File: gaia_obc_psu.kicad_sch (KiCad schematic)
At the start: 74 parts, among them IC1 MAX17048G+T10, Q2 FS8205A, SW8 SW_Slide_DPDT, U10 TPS22917DBV, U11 AP2112K-3.3, U12 DW01A, U13 AP2112K-3.0, U14 LGS4056HDB, U4 INA3221, U5 INA3221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

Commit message: obc v1.2-pre1
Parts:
- removed R43, R44, R45, R46, R47: 0, Resistor_SMD:R_0402_1005Metric, symbol Device:R_Small
- D10, D11: footprint LED_SMD:LED_0603_1608Metric -> LED_SMD:LED_0805_2012Metric
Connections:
- net at R49.1: now also D10.2 (A); no longer D10.1 (K)
- net at D11.1 (K): now also U14.6 (~{STDBY}); no longer R50.2
- net at D11.2 (A): now also R50.2; no longer U14.6 (~{STDBY})
- net at U14.7 (~{CHRG}): now also D10.1 (K); no longer D10.2 (A)

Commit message: v1.2
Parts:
- removed C33: 10uF, Capacitor_SMD:C_0603_1608Metric, symbol Device:C_Small
- removed IC1: MAX17048G+T10, gaia_obc-footprints:SON50P200X200X80-9N-D, symbol gaia_obc-symbols:MAX17048G+T10
- removed R54, R55: 100k, Resistor_SMD:R_0603_1608Metric, symbol Device:R_Small
- added C49: 1uF, Capacitor_SMD:C_0603_1608Metric, symbol Device:C_Small
- added R6: 0.01R, Resistor_SMD:R_2512_6332Metric, symbol Device:R_Small
- added U19: INA238/INA237, Package_SO:VSSOP-10_3x3mm_P0.5mm, symbol Sensor_Energy:INA238
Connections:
- net +3.3V: now also C49.1, U19.1 (A1), U19.2 (A0), U19.6 (VS)
- net +BATT: now also R6.2, U19.9 (Vin-)
- net GND: now also C49.2, U19.7 (GND)
- net I2C_1_SCL: now also U19.5 (SCL)
- net I2C_1_SDA: now also U19.4 (SDA)
- new net PRI_HI: R6.1, U19.10 (Vin+), U19.8 (Vbus)

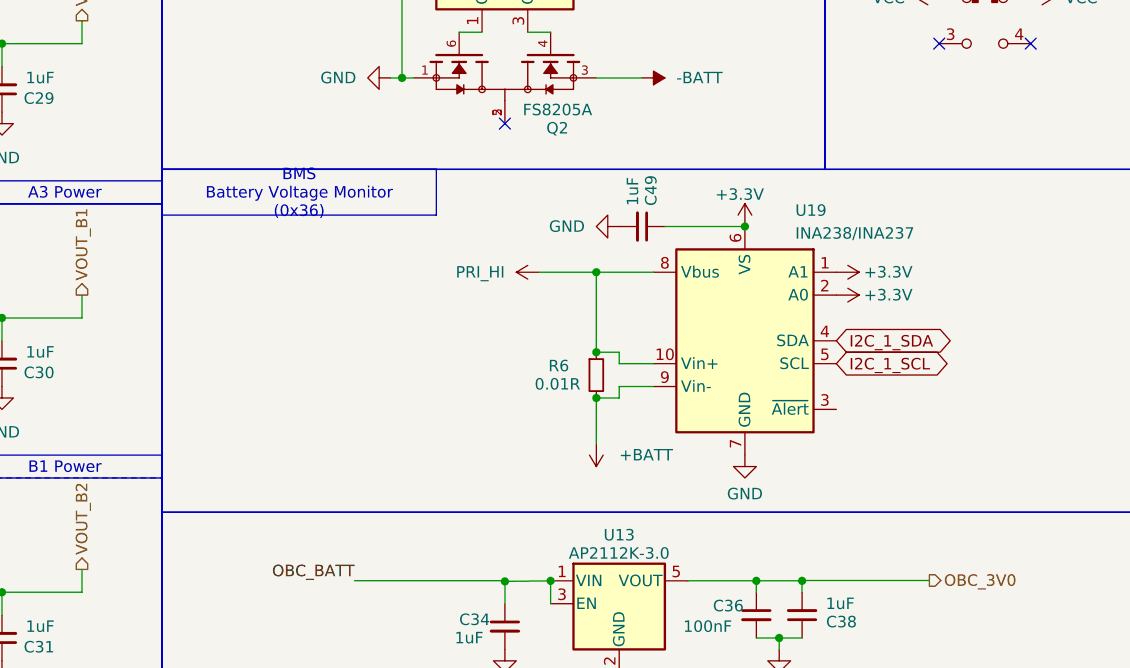
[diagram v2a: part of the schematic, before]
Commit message: adding logos + generating production files
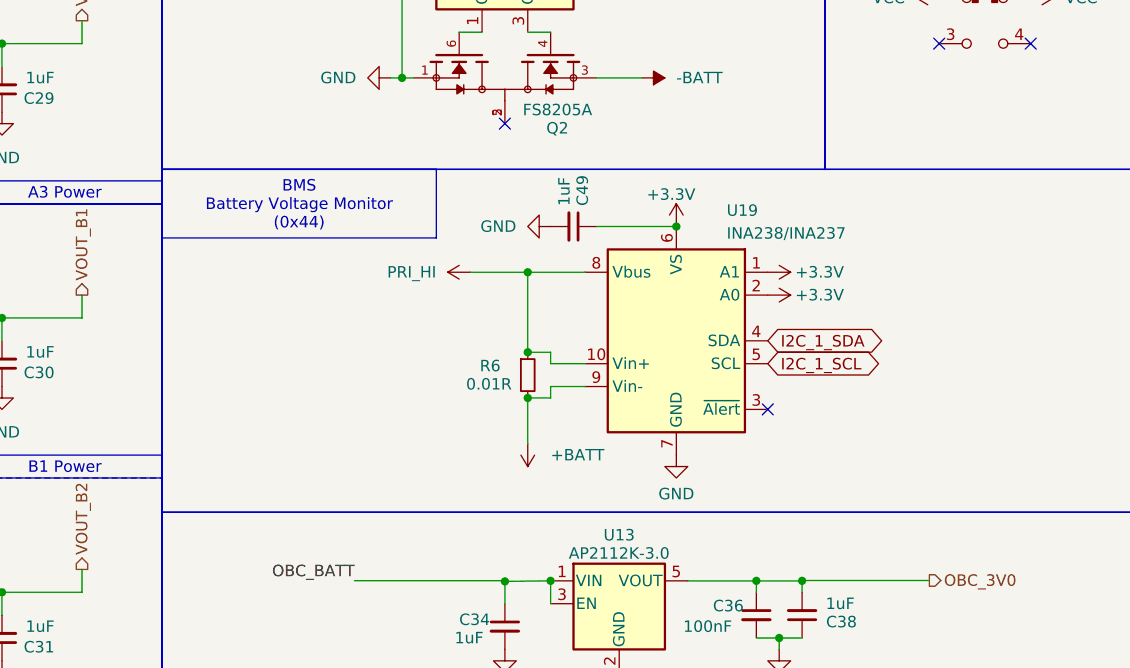
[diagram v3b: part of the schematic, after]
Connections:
- no-connect marks 3 -> 4
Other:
- moved on the sheet: C49, R6, U19

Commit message: v1.3
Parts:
- removed C32: 100nF, Capacitor_SMD:C_0402_1005Metric, symbol Device:C_Small
- removed C35, C37: 10uF, Capacitor_SMD:C_0603_1608Metric, symbol Device:C_Small
- removed C49: 1uF, Capacitor_SMD:C_0603_1608Metric, symbol Device:C_Small
- removed D10, D11: LED, LED_SMD:LED_0805_2012Metric, symbol Device:LED_Small
- removed Q2: FS8205A, gaia_obc-footprints:SOT-23-6, symbol OnionSAT_Gaia:FS8205A
- removed R48: 100, Resistor_SMD:R_0603_1608Metric, symbol Device:R_Small
- removed R49, R50: TBA, Resistor_SMD:R_0402_1005Metric, symbol Device:R_Small
- removed R51: 1k, Resistor_SMD:R_0603_1608Metric, symbol Device:R_Small
- removed R53: 1k, Resistor_SMD:R_0402_1005Metric, symbol Device:R_Small
- removed R6: 0.01R, Resistor_SMD:R_2512_6332Metric, symbol Device:R_Small
- removed SW8: SW_Slide_DPDT, gaia_obc-footprints:MS-22D28-G020, symbol Switch:SW_Slide_DPDT
- removed U12: DW01A, gaia_obc-footprints:SOT-23-6, symbol Battery_Management:DW01A
- removed U14: LGS4056HDB, gaia_obc-footprints:DFN-8-1EP_3x3mm_P0.65mm_EP1.55x2.4mm, symbol gaia_obc-symbols:LGS4056HDB
- removed U19: INA238/INA237, Package_SO:VSSOP-10_3x3mm_P0.5mm, symbol Sensor_Energy:INA238
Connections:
- no-connect marks 4 -> 0

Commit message: neptune 1.3 production
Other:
- title: GAIA On-Board Computer -> Neptune On-Board Computer
- moved on the sheet: C34, C36, C38, U13
